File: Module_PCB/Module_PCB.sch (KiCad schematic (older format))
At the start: 105 parts, among them J1 ISP, J2 US, J3 DS, Q1 HSS2307, Q2 BSS123, U1 W25Q16JV, U2 AP1117-33, U3 TPS563200, U5 ATmega328P-AU, U7 74LVC1G34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

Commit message: Changed 10k and 15k resistors to 1% variants
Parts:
- R1, R2, R4, R5, R7, R8: MPN RC0603JR-0710KL -> RC0603FR-0710KL
- R10: MPN RC0603JR-0715KL -> RC0603FR-0715KL
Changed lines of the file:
@@
 F 2 "Resistor_SMD:R_0603_1608Metric" V 580 4950 50  0001 C CNN
 F 3 "~" H 650 4950 50  0001 C CNN
-F 4 "RC0603JR-0710KL" H 650 4950 50  0001 C CNN "MPN"
+F 4 "RC0603FR-0710KL" H 650 4950 50  0001 C CNN "MPN"
 F 5 "YAGEO" H 650 4950 50  0001 C CNN "Manufacturer"
 	1    650  4950
@@
 F 2 "Resistor_SMD:R_0603_1608Metric" V 1730 6550 50  0001 C CNN
 F 3 "~" H 1800 6550 50  0001 C CNN
-F 4 "RC0603JR-0710KL" H 1800 6550 50  0001 C CNN "MPN"
+F 4 "RC0603FR-0710KL" H 1800 6550 50  0001 C CNN "MPN"
 F 5 "YAGEO" H 1800 6550 50  0001 C CNN "Manufacturer"
 	1    1800 6550
@@
 F 2 "Resistor_SMD:R_0603_1608Metric" V 2380 3350 50  0001 C CNN
 F 3 "~" H 2450 3350 50  0001 C CNN
-F 4 "RC0603JR-0710KL" H 2450 3350 50  0001 C CNN "MPN"
+F 4 "RC0603FR-0710KL" H 2450 3350 50  0001 C CNN "MPN"
 F 5 "YAGEO" H 2450 3350 50  0001 C CNN "Manufacturer"
 	1    2450 3350
@@
 F 3 "~" H 2150 1250 50  0001 C CNN
 F 4 "YAGEO" H 2150 1250 50  0001 C CNN "Manufacturer"
-F 5 "RC0603JR-0710KL" H 2150 1250 50  0001 C CNN "MPN"
+F 5 "RC0603FR-0710KL" H 2150 1250 50  0001 C CNN "MPN"
 	1    2150 1250
 	1    0    0    -1
@@
 F 3 "~" H 2950 1850 50  0001 C CNN
 F 4 "YAGEO" H 2950 1850 50  0001 C CNN "Manufacturer"
-F 5 "RC0603JR-0710KL" H 2950 1850 50  0001 C CNN "MPN"
+F 5 "RC0603FR-0710KL" H 2950 1850 50  0001 C CNN "MPN"
 	1    2950 1850
 	1    0    0    -1
@@
 F 3 "~" H 3750 1550 50  0001 C CNN
 F 4 "YAGEO" H 3750 1550 50  0001 C CNN "Manufacturer"
-F 5 "RC0603JR-0715KL" H 3750 1550 50  0001 C CNN "MPN"
+F 5 "RC0603FR-0715KL" H 3750 1550 50  0001 C CNN "MPN"
 	1    3750 1550
 	1    0    0    -1
@@
 F 3 "~" H 3750 1150 50  0001 C CNN
 F 4 "YAGEO" H 3750 1150 50  0001 C CNN "Manufacturer"
-F 5 "RC0603JR-0710KL" H 3750 1150 50  0001 C CNN "MPN"
+F 5 "RC0603FR-0710KL" H 3750 1150 50  0001 C CNN "MPN"
 	1    3750 1150
 	1    0    0    -1

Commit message: Added MPN for 3x2 angled inter-module connectors
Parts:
- J2: MPN (none) -> PZ254R-12-6P; Manufacturer (none) -> XFCN
- J3: MPN (none) -> C576162; Manufacturer (none) -> BOOMELE
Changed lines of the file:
@@
 F 2 "Connector_PinSocket_2.54mm:PinSocket_2x03_P2.54mm_Horizontal" H 4100 4300 50  0001 C CNN
 F 3 "~" H 4100 4300 50  0001 C CNN
+F 4 "BOOMELE" H 4100 4300 50  0001 C CNN "Manufacturer"
+F 5 "C576162" H 4100 4300 50  0001 C CNN "MPN"
 	1    4100 4300
 	1    0    0    -1
@@
 F 2 "Connector_PinHeader_2.54mm:PinHeader_2x03_P2.54mm_Horizontal" H 4100 3700 50  0001 C CNN
 F 3 "~" H 4100 3700 50  0001 C CNN
+F 4 "XFCN" H 4100 3700 50  0001 C CNN "Manufacturer"
+F 5 "PZ254R-12-6P" H 4100 3700 50  0001 C CNN "MPN"
 	1    4100 3700
 	1    0    0    -1

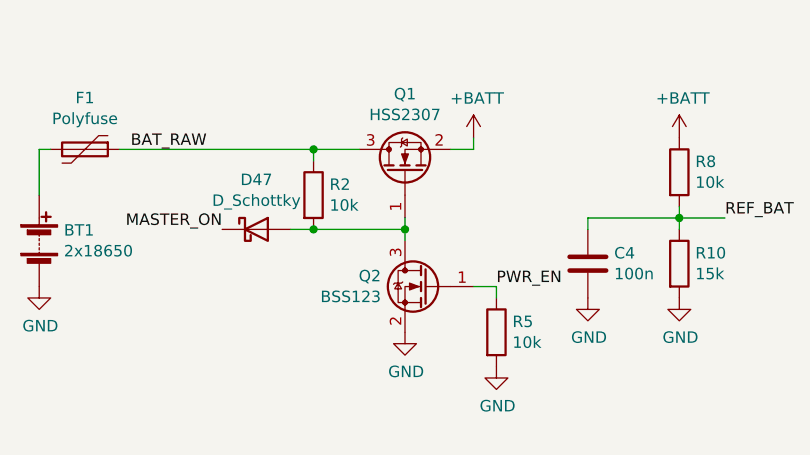
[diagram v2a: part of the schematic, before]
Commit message: Fixed wrong symbol, wrong pinout, and wrong footprint of p-channel power mosfet
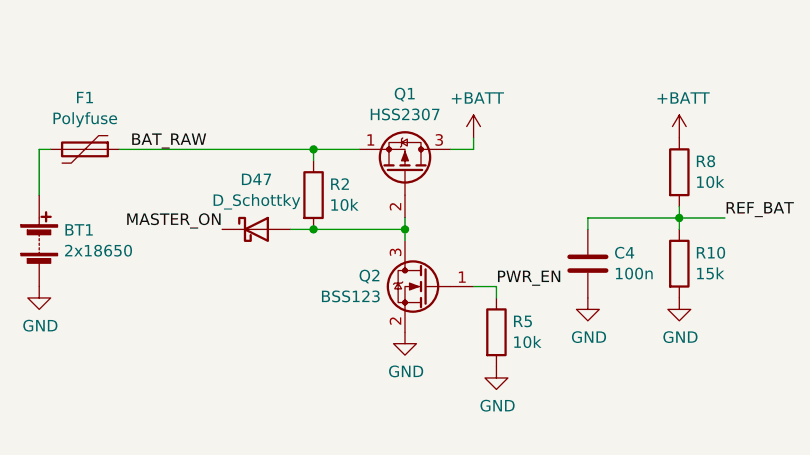
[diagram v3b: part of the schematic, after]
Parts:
- removed Q1: HSS2307, Package_TO_SOT_SMD:SOT-23, symbol Device:Q_NMOS_GSD
- added Q1: HSS2307, Package_TO_SOT_SMD:SOT-23W, symbol Device:Q_PMOS_SGD
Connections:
- net +BATT: now also Q1.3 (D)
- net BAT_RAW: now also Q1.1 (S)
- net at D47.2 (A), Q2.3 (D), R2.2: now also Q1.2 (G)
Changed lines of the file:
@@
 	4650 6100 4650 6150
-$Comp
-L Device:Q_NMOS_GSD Q1
-U 1 1 60DA7D36
-P 2550 1150
-F 0 "Q1" V 2892 1150 50  0000 C CNN
-F 1 "HSS2307" V 2801 1150 50  0000 C CNN
-F 2 "Package_TO_SOT_SMD:SOT-23" H 2750 1250 50  0001 C CNN
-F 3 "~" H 2550 1150 50  0001 C CNN
-F 4 "Huashuo" H 2550 1150 50  0001 C CNN "Manufacturer"
-F 5 "HSS2307" H 2550 1150 50  0001 C CNN "MPN"
-	1    2550 1150
-	0    -1   -1   0
-$EndComp
 $Comp
 L Transistor_FET:BSS123 Q2
@@
 Wire Wire Line
 	3350 1350 3350 1400
+$Comp
+L Device:Q_PMOS_SGD Q1
+U 1 1 60F2C1CF
+P 2550 1150
+F 0 "Q1" V 2892 1150 50  0000 C CNN
+F 1 "HSS2307" V 2801 1150 50  0000 C CNN
+F 2 "Package_TO_SOT_SMD:SOT-23W" H 2750 1250 50  0001 C CNN
+F 3 "~" H 2550 1150 50  0001 C CNN
+F 4 "HSS2307" H 2550 1150 50  0001 C CNN "MPN"
+F 5 "Huashuo" H 2550 1150 50  0001 C CNN "Manufacturer"
+	1    2550 1150
+	0    1    -1   0
+$EndComp
 $EndSCHEMATC

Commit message: Fixed missing PWR_EN signal
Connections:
- net PWR_EN: now also U5.27 (PC4)
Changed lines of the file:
@@
 	0    1    -1   0
 $EndComp
+Text Label 3200 6000 0    50   ~ 0
+PWR_EN
 $EndSCHEMATC

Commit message: Fixed wrong connection between TX and RETO/RETI
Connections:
- net RETI: now also R12.2
- net RETO: no longer R12.2
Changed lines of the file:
@@
 Text Label 5350 6850 2    50   ~ 0
-RETO
-Text Label 5350 7500 2    50   ~ 0
 RETO
 Text Label 4100 5900 2    50   ~ 0
@@
 Text Label 3200 6000 0    50   ~ 0
 PWR_EN
+Text Label 5350 7500 2    50   ~ 0
+RETI
 $EndSCHEMATC

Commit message: Added pull-up for RETI to ensure high-level uart signal when no module follows and the return path is currently disabled
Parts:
- added R14: 10k, Resistor_SMD:R_0603_1608Metric, symbol Device:R
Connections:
- net +3V3: now also R14.1
- net RETI: now also R14.2
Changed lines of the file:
@@
 Text Label 5350 7500 2    50   ~ 0
 RETI
+$Comp
+L Device:R R14
+U 1 1 60F1E619
+P 6650 6650
+F 0 "R14" H 6720 6696 50  0000 L CNN
+F 1 "10k" H 6720 6605 50  0000 L CNN
+F 2 "Resistor_SMD:R_0603_1608Metric" V 6580 6650 50  0001 C CNN
+F 3 "~" H 6650 6650 50  0001 C CNN
+F 4 "RC0603FR-0710KL" H 6650 6650 50  0001 C CNN "MPN"
+F 5 "YAGEO" H 6650 6650 50  0001 C CNN "Manufacturer"
+	1    6650 6650
+	1    0    0    -1
+$EndComp
+$Comp
+L power:+3V3 #PWR0140
+U 1 1 60F1ECF3
+P 6650 6500
+F 0 "#PWR0140" H 6650 6350 50  0001 C CNN
+F 1 "+3V3" H 6665 6673 50  0000 C CNN
+F 2 "" H 6650 6500 50  0001 C CNN
+F 3 "" H 6650 6500 50  0001 C CNN
+	1    6650 6500
+	1    0    0    -1
+$EndComp
+Text Label 6650 6800 3    50   ~ 0
+RETI
 $EndSCHEMATC

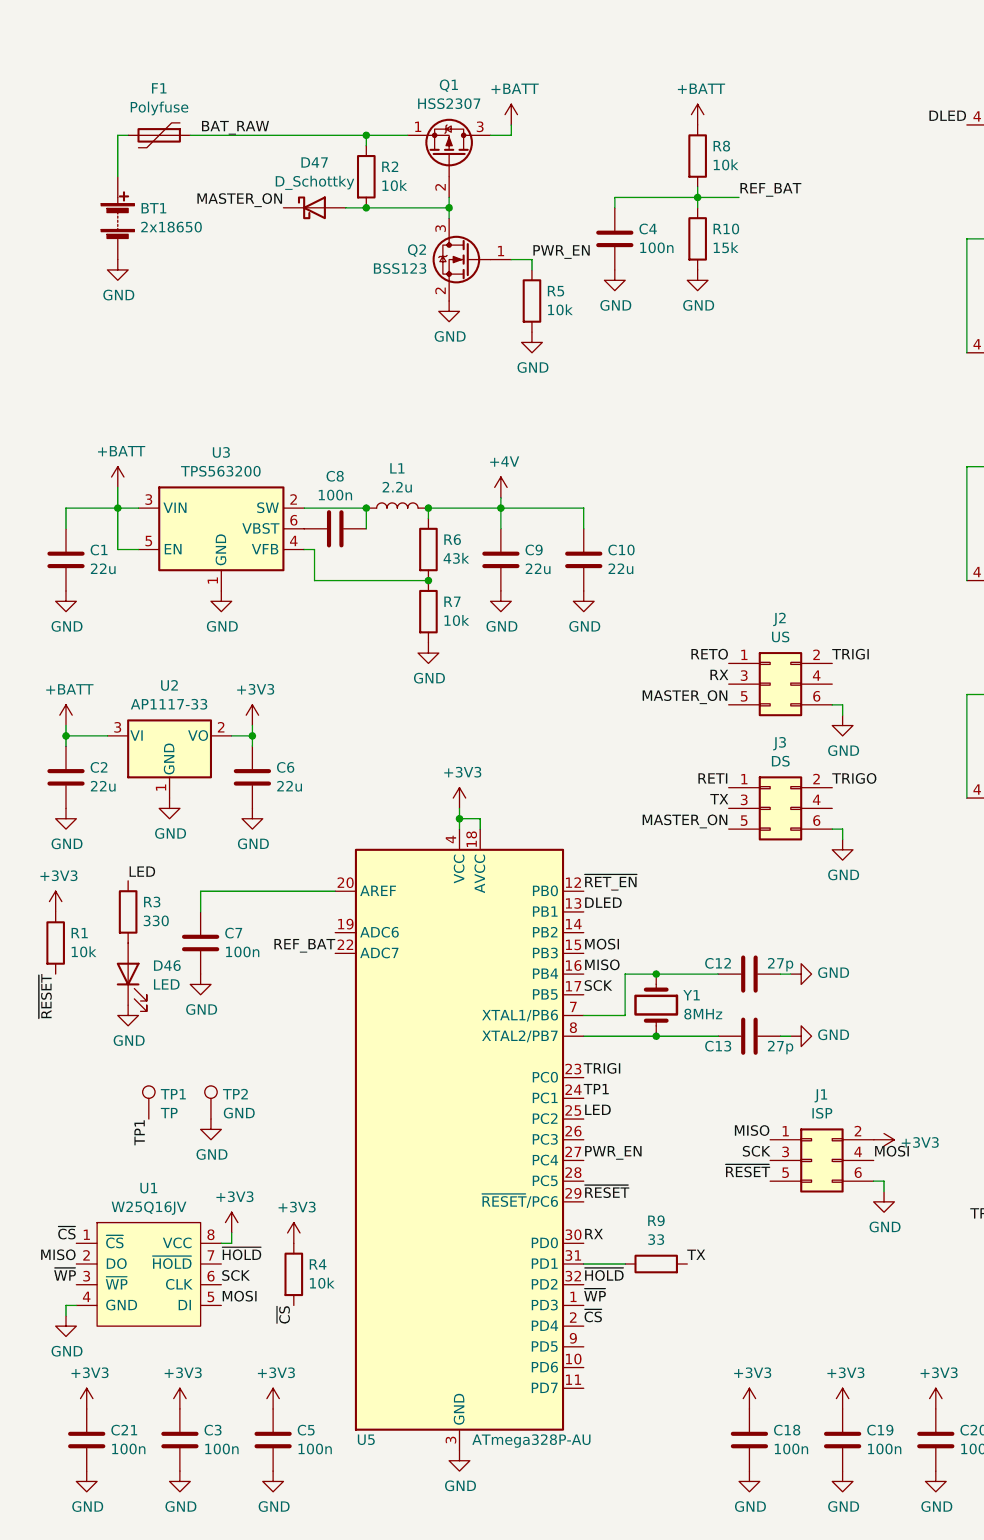
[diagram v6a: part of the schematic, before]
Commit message: Fixed ERC errors by adding nc and power indicators
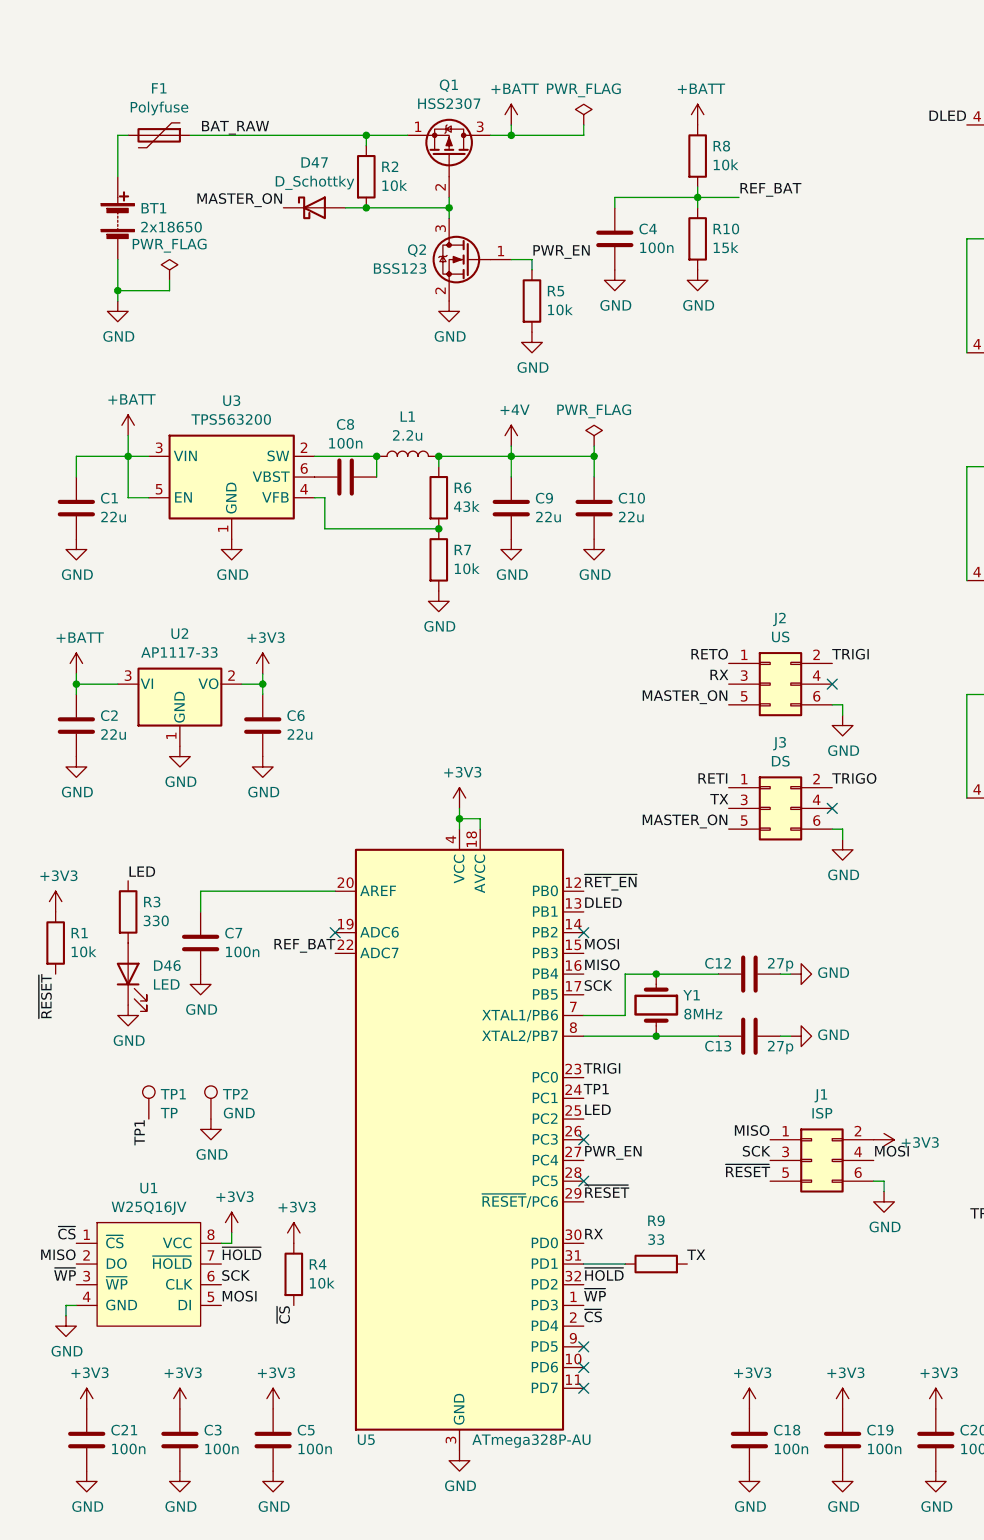
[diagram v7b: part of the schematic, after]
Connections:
- no-connect marks 7 -> 16
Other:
- moved on the sheet: C1, C10, C2, C6, C8, C9, L1, R6, R7, U2, U3

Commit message: Updated 22u capacitors to 1206 package
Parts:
- C1, C10, C14, C15, C16, C17, C2, C22, C6, C9: footprint Capacitor_SMD:C_0603_1608Metric -> Capacitor_SMD:C_1206_3216Metric; MPN CC0603MRX5R5BB226 -> CC1206KKX5R8BB226
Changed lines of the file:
@@
 F 0 "C6" H 1765 3946 50  0000 L CNN
 F 1 "22u" H 1765 3855 50  0000 L CNN
-F 2 "Capacitor_SMD:C_0603_1608Metric" H 1688 3750 50  0001 C CNN
+F 2 "Capacitor_SMD:C_1206_3216Metric" H 1688 3750 50  0001 C CNN
 F 3 "~" H 1650 3900 50  0001 C CNN
-F 4 "CC0603MRX5R5BB226" H 1650 3900 50  0001 C CNN "MPN"
+F 4 "CC1206KKX5R8BB226" H 1650 3900 50  0001 C CNN "MPN"
 F 5 "YAGEO" H 1650 3900 50  0001 C CNN "Manufacturer"
 	1    1650 3900
@@
 F 0 "C2" H 865 3946 50  0000 L CNN
 F 1 "22u" H 865 3855 50  0000 L CNN
-F 2 "Capacitor_SMD:C_0603_1608Metric" H 788 3750 50  0001 C CNN
+F 2 "Capacitor_SMD:C_1206_3216Metric" H 788 3750 50  0001 C CNN
 F 3 "~" H 750 3900 50  0001 C CNN
-F 4 "CC0603MRX5R5BB226" H 750 3900 50  0001 C CNN "MPN"
+F 4 "CC1206KKX5R8BB226" H 750 3900 50  0001 C CNN "MPN"
 F 5 "YAGEO" H 750 3900 50  0001 C CNN "Manufacturer"
 	1    750  3900
@@
 F 0 "C9" H 2965 2896 50  0000 L CNN
 F 1 "22u" H 2965 2805 50  0000 L CNN
-F 2 "Capacitor_SMD:C_0603_1608Metric" H 2888 2700 50  0001 C CNN
+F 2 "Capacitor_SMD:C_1206_3216Metric" H 2888 2700 50  0001 C CNN
 F 3 "~" H 2850 2850 50  0001 C CNN
-F 4 "CC0603MRX5R5BB226" H 2850 2850 50  0001 C CNN "MPN"
+F 4 "CC1206KKX5R8BB226" H 2850 2850 50  0001 C CNN "MPN"
 F 5 "YAGEO" H 2850 2850 50  0001 C CNN "Manufacturer"
 	1    2850 2850
@@
 F 0 "C1" H 865 2896 50  0000 L CNN
 F 1 "22u" H 865 2805 50  0000 L CNN
-F 2 "Capacitor_SMD:C_0603_1608Metric" H 788 2700 50  0001 C CNN
+F 2 "Capacitor_SMD:C_1206_3216Metric" H 788 2700 50  0001 C CNN
 F 3 "~" H 750 2850 50  0001 C CNN
-F 4 "CC0603MRX5R5BB226" H 750 2850 50  0001 C CNN "MPN"
+F 4 "CC1206KKX5R8BB226" H 750 2850 50  0001 C CNN "MPN"
 F 5 "YAGEO" H 750 2850 50  0001 C CNN "Manufacturer"
 	1    750  2850
@@
 F 0 "C10" H 3365 2896 50  0000 L CNN
 F 1 "22u" H 3365 2805 50  0000 L CNN
-F 2 "Capacitor_SMD:C_0603_1608Metric" H 3288 2700 50  0001 C CNN
+F 2 "Capacitor_SMD:C_1206_3216Metric" H 3288 2700 50  0001 C CNN
 F 3 "~" H 3250 2850 50  0001 C CNN
-F 4 "CC0603MRX5R5BB226" H 3250 2850 50  0001 C CNN "MPN"
+F 4 "CC1206KKX5R8BB226" H 3250 2850 50  0001 C CNN "MPN"
 F 5 "YAGEO" H 3250 2850 50  0001 C CNN "Manufacturer"
 	1    3250 2850
@@
 F 0 "C16" H 9965 6146 50  0000 L CNN
 F 1 "22u" H 9965 6055 50  0000 L CNN
-F 2 "Capacitor_SMD:C_0603_1608Metric" H 9888 5950 50  0001 C CNN
+F 2 "Capacitor_SMD:C_1206_3216Metric" H 9888 5950 50  0001 C CNN
 F 3 "~" H 9850 6100 50  0001 C CNN
-F 4 "CC0603MRX5R5BB226" H 9850 6100 50  0001 C CNN "MPN"
+F 4 "CC1206KKX5R8BB226" H 9850 6100 50  0001 C CNN "MPN"
 F 5 "YAGEO" H 9850 6100 50  0001 C CNN "Manufacturer"
 	1    9850 6100
@@
 F 0 "C17" H 10565 6146 50  0000 L CNN
 F 1 "22u" H 10565 6055 50  0000 L CNN
-F 2 "Capacitor_SMD:C_0603_1608Metric" H 10488 5950 50  0001 C CNN
+F 2 "Capacitor_SMD:C_1206_3216Metric" H 10488 5950 50  0001 C CNN
 F 3 "~" H 10450 6100 50  0001 C CNN
-F 4 "CC0603MRX5R5BB226" H 10450 6100 50  0001 C CNN "MPN"
+F 4 "CC1206KKX5R8BB226" H 10450 6100 50  0001 C CNN "MPN"
 F 5 "YAGEO" H 10450 6100 50  0001 C CNN "Manufacturer"
 	1    10450 6100
@@
 F 0 "C14" H 8765 6146 50  0000 L CNN
 F 1 "22u" H 8765 6055 50  0000 L CNN
-F 2 "Capacitor_SMD:C_0603_1608Metric" H 8688 5950 50  0001 C CNN
+F 2 "Capacitor_SMD:C_1206_3216Metric" H 8688 5950 50  0001 C CNN
 F 3 "~" H 8650 6100 50  0001 C CNN
-F 4 "CC0603MRX5R5BB226" H 8650 6100 50  0001 C CNN "MPN"
+F 4 "CC1206KKX5R8BB226" H 8650 6100 50  0001 C CNN "MPN"
 F 5 "YAGEO" H 8650 6100 50  0001 C CNN "Manufacturer"
 	1    8650 6100
@@
 F 0 "C15" H 9365 6146 50  0000 L CNN
 F 1 "22u" H 9365 6055 50  0000 L CNN
-F 2 "Capacitor_SMD:C_0603_1608Metric" H 9288 5950 50  0001 C CNN
+F 2 "Capacitor_SMD:C_1206_3216Metric" H 9288 5950 50  0001 C CNN
 F 3 "~" H 9250 6100 50  0001 C CNN
-F 4 "CC0603MRX5R5BB226" H 9250 6100 50  0001 C CNN "MPN"
+F 4 "CC1206KKX5R8BB226" H 9250 6100 50  0001 C CNN "MPN"
 F 5 "YAGEO" H 9250 6100 50  0001 C CNN "Manufacturer"
 	1    9250 6100
@@
 F 0 "C22" H 8165 6146 50  0000 L CNN
 F 1 "22u" H 8165 6055 50  0000 L CNN
-F 2 "Capacitor_SMD:C_0603_1608Metric" H 8088 5950 50  0001 C CNN
+F 2 "Capacitor_SMD:C_1206_3216Metric" H 8088 5950 50  0001 C CNN
 F 3 "~" H 8050 6100 50  0001 C CNN
-F 4 "CC0603MRX5R5BB226" H 8050 6100 50  0001 C CNN "MPN"
+F 4 "CC1206KKX5R8BB226" H 8050 6100 50  0001 C CNN "MPN"
 F 5 "YAGEO" H 8050 6100 50  0001 C CNN "Manufacturer"
 	1    8050 6100
